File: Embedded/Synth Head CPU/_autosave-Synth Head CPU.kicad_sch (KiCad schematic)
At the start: 17 parts, among them J1 10171746-00021LF, J2 JST [C], U5 FFC [G], U6 FFC [M], U7 FFC [K], U8 NEO-M8M

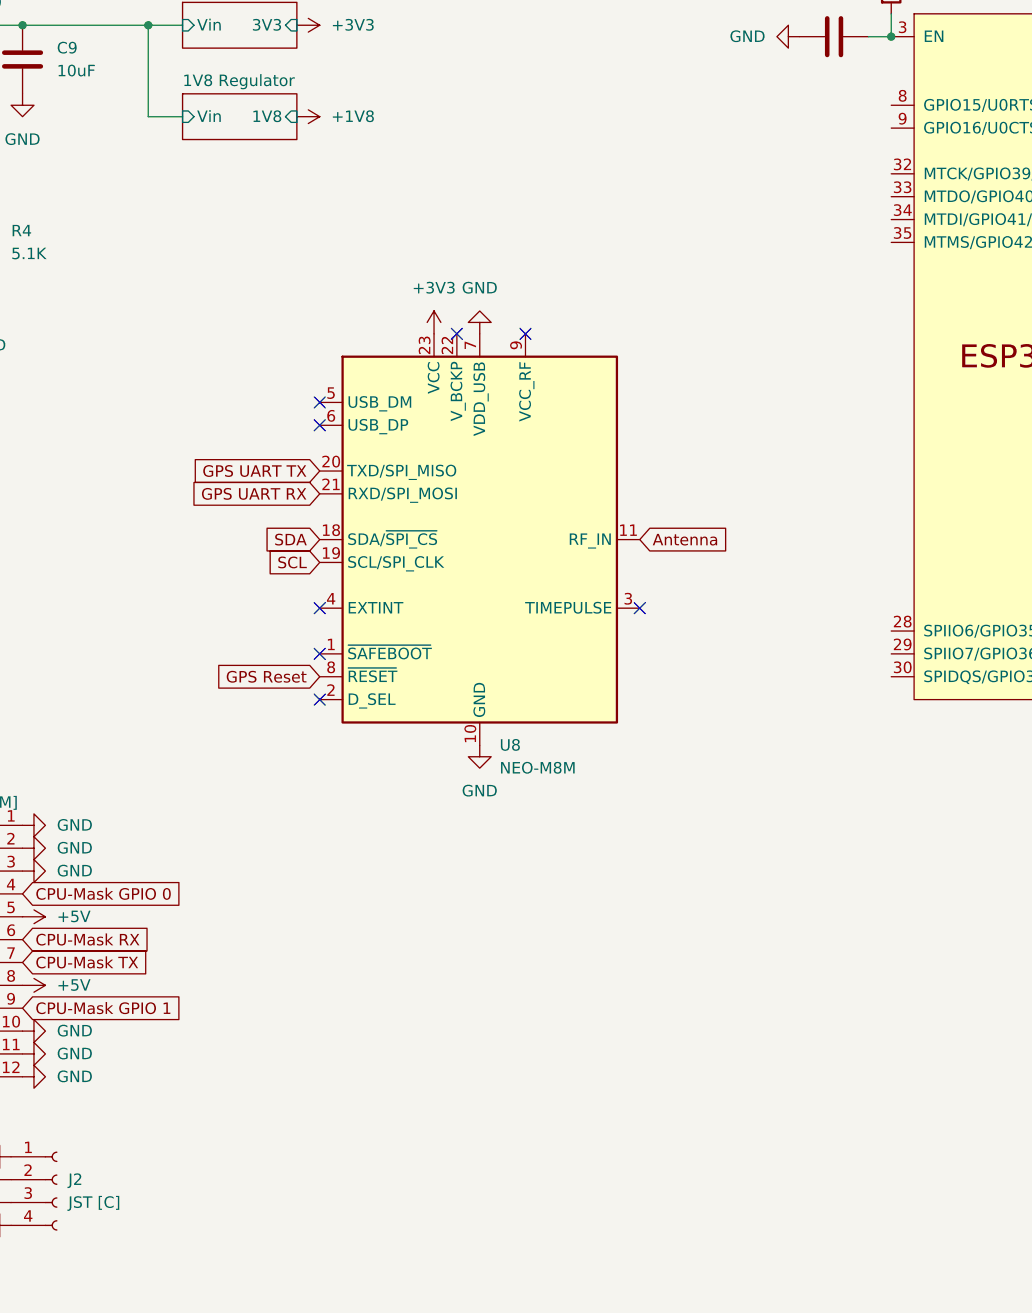
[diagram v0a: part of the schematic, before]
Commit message: Added GPS & Micro SD Card
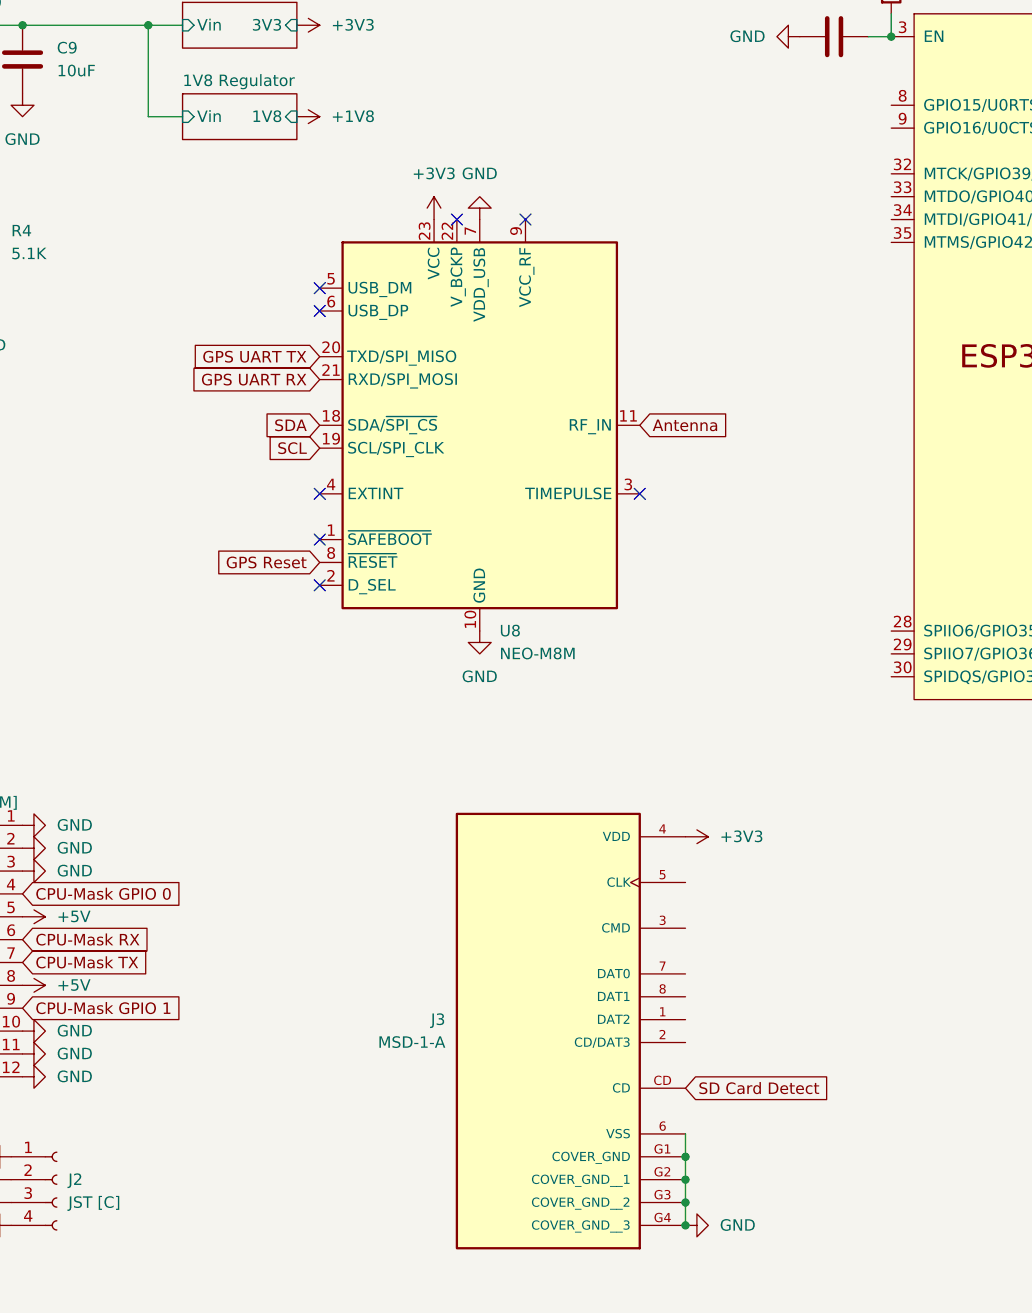
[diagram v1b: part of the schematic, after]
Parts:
- added J3: MSD-1-A, MSD-1-A:CUI_MSD-1-A, symbol MicroSD_MSD_1_A:MSD-1-A
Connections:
- net +3V3: now also J3.4 (VDD)
- net GND: now also J3.6 (VSS), J3.G1 (COVER_GND), J3.G2 (COVER_GND__1), J3.G3 (COVER_GND__2), J3.G4 (COVER_GND__3)
- new net SD Card Detect: J3.CD
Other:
- moved on the sheet: U8
